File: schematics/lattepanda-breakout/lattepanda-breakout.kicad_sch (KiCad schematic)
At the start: 8 parts, among them J1 RJ45, J3 Conn_02x04_Odd_Even, J4 Conn_02x15_Odd_Even, J5 Conn_02x02_Odd_Even, J6 Conn_01x03_Socket, J7 Conn_01x03_Socket, J8 Conn_01x03_Socket, J9 Conn_01x03_Socket

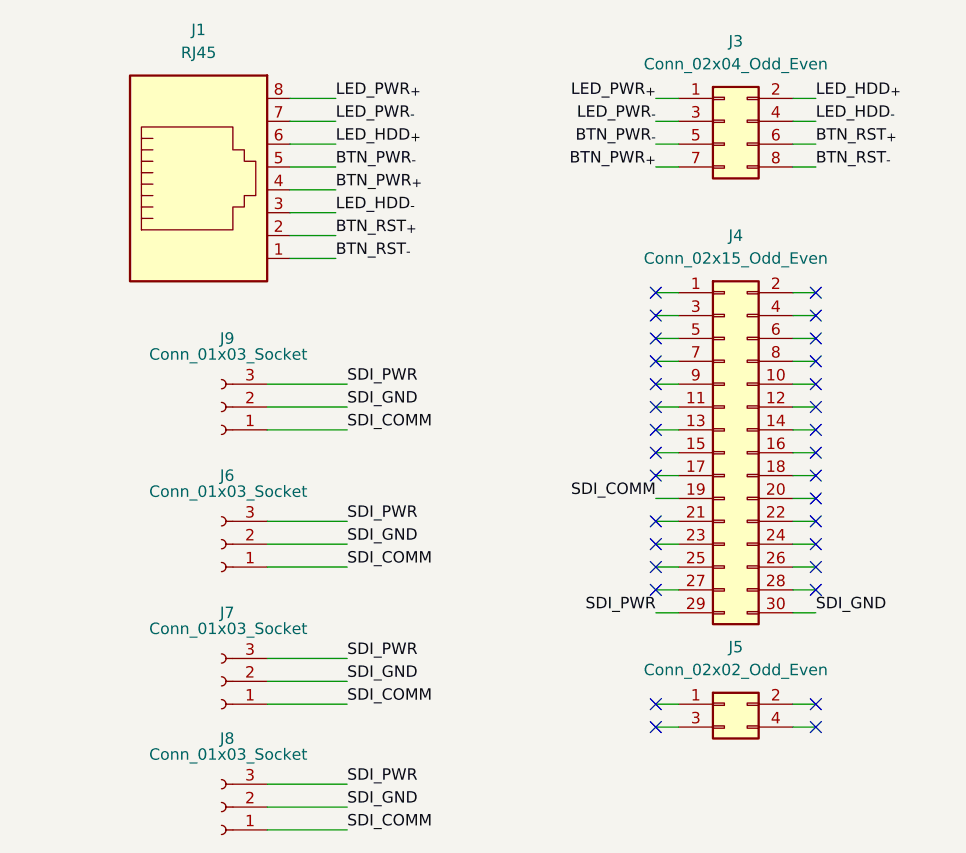
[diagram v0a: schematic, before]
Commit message: open up sata
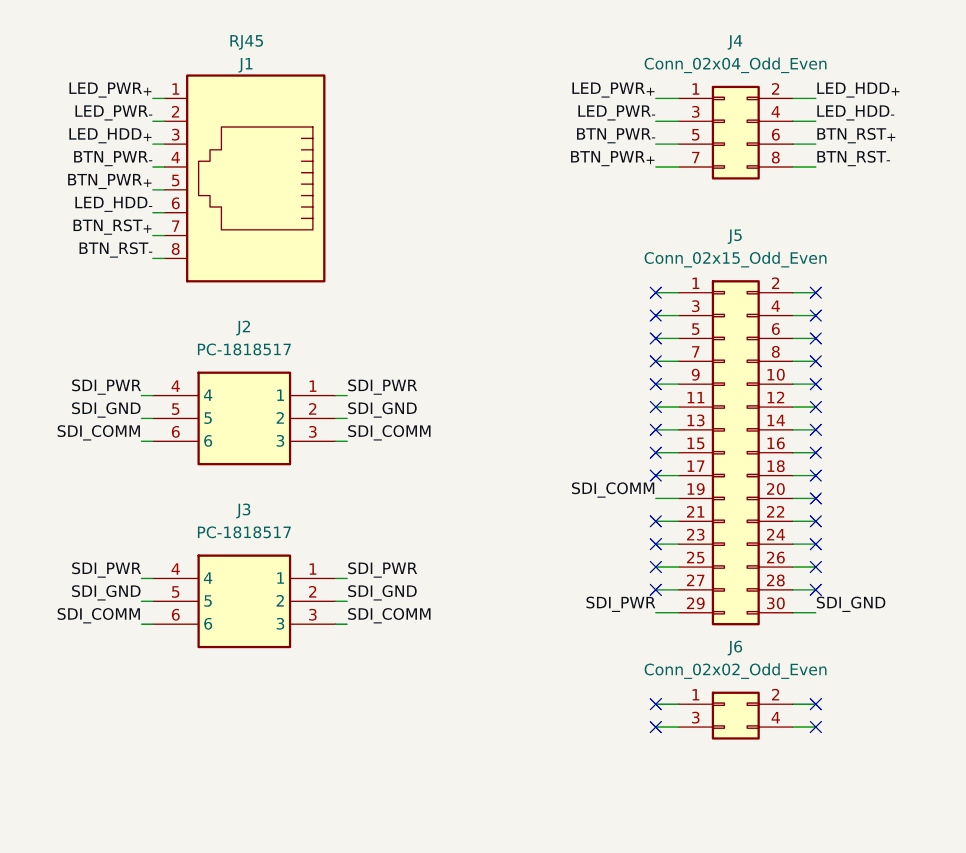
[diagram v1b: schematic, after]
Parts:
- removed J6, J7, J8, J9: Conn_01x03_Socket, Link_Footprints:PC-1844223, symbol Connector:Conn_01x03_Socket
- added J2, J3: PC-1818517, Link_Footprints:PC-1818517, symbol Link_Components:PC-1818517
- renumbered J3 to J4, J4 to J5, J5 to J6
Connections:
- net BTN_PWR_{+}: now also J1.5; no longer J1.4
- net BTN_PWR_{-}: now also J1.4; no longer J1.5
- net BTN_RST_{+}: now also J1.7; no longer J1.2
- net BTN_RST_{-}: now also J1.8; no longer J1.1
- net LED_HDD_{+}: now also J1.3; no longer J1.6
- net LED_HDD_{-}: now also J1.6; no longer J1.3
- net LED_PWR_{+}: now also J1.1; no longer J1.8
- net LED_PWR_{-}: now also J1.2; no longer J1.7
- net SDI_COMM: now also J2.3, J2.6, J3.3, J3.6
- net SDI_GND: now also J2.2, J2.5, J3.2, J3.5
- net SDI_PWR: now also J2.1, J2.4, J3.1, J3.4
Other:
- moved on the sheet: J1
